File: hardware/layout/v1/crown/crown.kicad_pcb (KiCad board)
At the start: 4 copper layers, 41 x 56 mm, 46 parts, among them J1 Main board, J2 XD_NORTH, J3 XD_EAST, J4 XD_SOUTH, J5 XD_WEST, J6 PIEZO_RAIN, U1 SN74LVC2G04, U2 CD4052BM96, U3 TLV9062IDR, U4 LM393DR2G, U5 TLV9062IDR, U6 LTR-390UV-01, U7 VEML7700-TT, U8 LIS2MDLTR

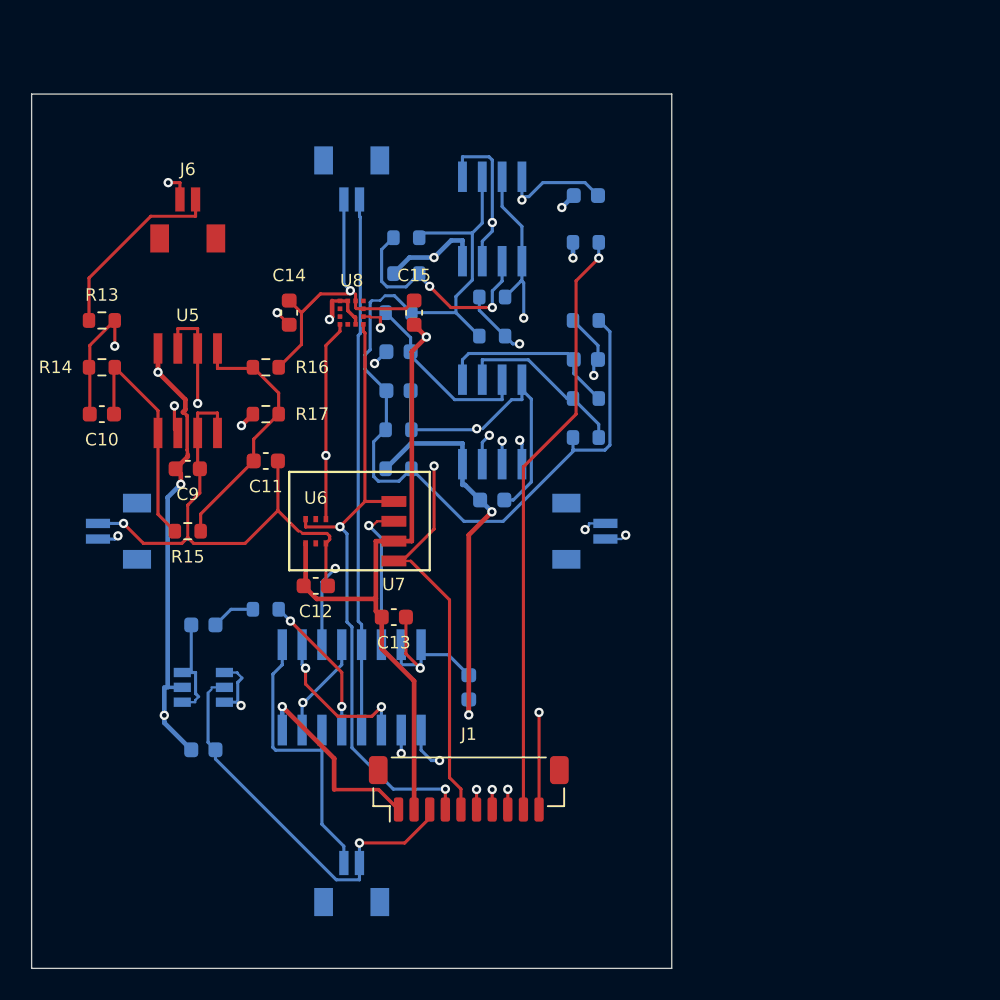
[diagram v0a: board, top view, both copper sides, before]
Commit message: Update project documentation and refactor crown sensor board circuit implementation
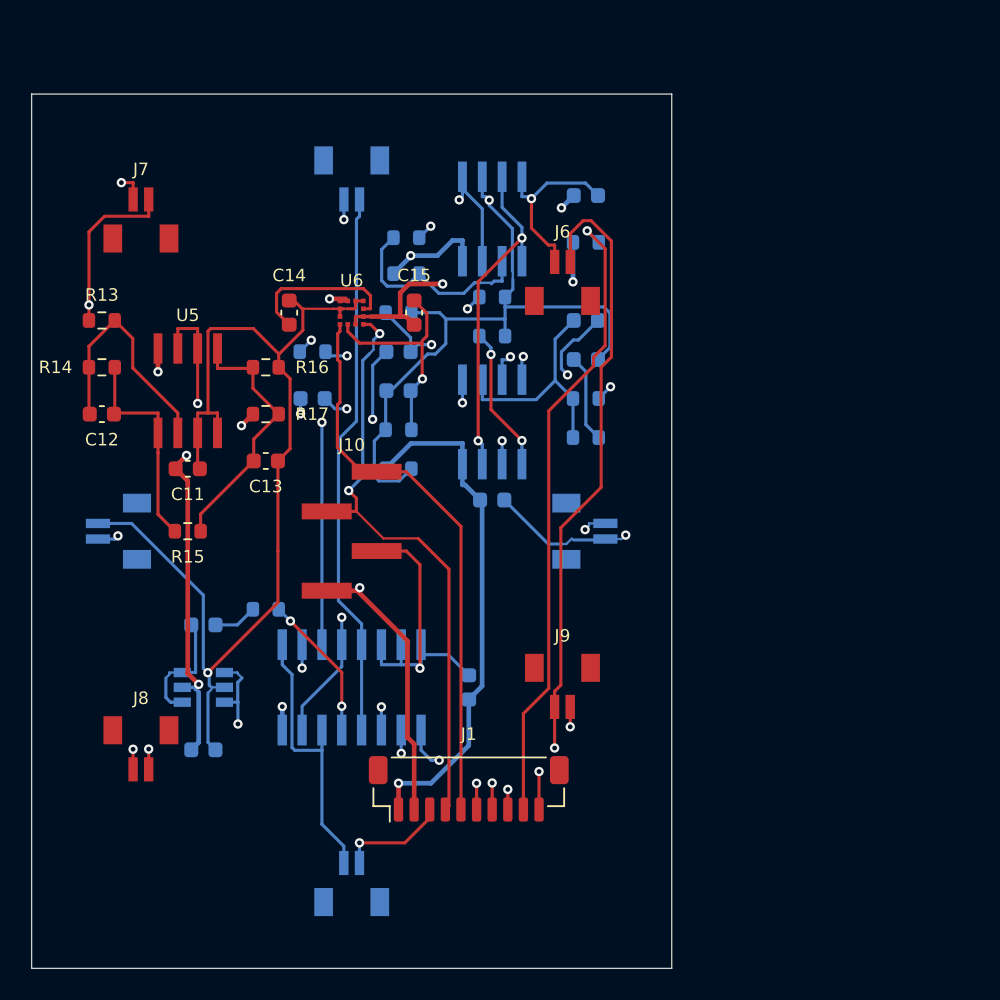
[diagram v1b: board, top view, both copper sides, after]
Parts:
- removed U7: VEML7700-TT, gateway_fp:Vishay_VEML7700-TT
- removed U8: LIS2MDLTR, gateway_fp:ST_LIS2MDLTR_LGA-12
- added J10: DOME_RISER, gateway_fp:HX_PZ2.54-1x4P-SMD, F.Cu at (20.5, -28.0)
- added J7: PIEZO_NW, gateway_fp:JST_BM02B-SRSS-TB, F.Cu at (7.00, -48.0)
- added J8: PIEZO_SW, gateway_fp:JST_BM02B-SRSS-TB, F.Cu at (7.00, -14.0)
- added J9: PIEZO_SE, gateway_fp:JST_BM02B-SRSS-TB, F.Cu at (34.0, -18.0)
- C10: value 47n 50V -> 100n 50V; moved to B.Cu
- C11: value 220n 50V -> 100n 50V
- C12, C8: value 100n 50V -> 18p C0G 50V
- C13: value 100n 50V -> 220n 50V
- C5: value 47n 50V -> 100n 50V
- C6: value 100n 50V -> 47n 50V
- C9: value 100n 50V -> 47n 50V; moved to B.Cu
- J2: value XD_NORTH -> XD_North
- J3: value XD_EAST -> XD_East
- J4: value XD_SOUTH -> XD_South
- J5: value XD_WEST -> XD_West
- J6: value PIEZO_RAIN -> PIEZO_NE
- U1: value SN74LVC2G04 -> SN74LVC2G04DBVR
- U6: value LTR-390UV-01 -> LIS2MDLTR; footprint gateway_fp:LiteOn_LTR-390UV-01 -> gateway_fp:ST_LIS2MDLTR_LGA-12
- moved C10 34.0 mm to (35.5, -49.5)
- moved J6 24.3 mm to (34.0, -44.0)
- moved C12 17.6 mm to (4.50, -35.5)
- moved U6 14.2 mm to (20.5, -42.0)
- moved C13 12.9 mm to (15.0, -32.5)
- moved R9 12.0 mm to (18.0, -39.5)
- moved C5 11.2 mm to (29.5, -30.0)
- moved C6 11.2 mm to (23.5, -39.5)
- moved C9 9.18 mm to (18.0, -36.5)
- moved C8 8.00 mm to (35.5, -41.5)
- moved R7 6.08 mm to (29.5, -40.5)
- moved C11 5.02 mm to (10.0, -32.0)
- moved R8 2.50 mm to (29.5, -43.0)
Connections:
- C10 pad 1: PIEZO_INV -> +5V
- C10 pad 2: PIEZO_STG1 -> GND
- C11 pad 1: PIEZO_ENV -> +5V
- C12 pad 1: +3V3 -> PIEZO_INV
- C12 pad 2: GND -> PIEZO_STG1
- C13 pad 1: +3V3 -> PIEZO_ENV
- C5 pad 1: US_RX_MUX -> +5V
- C5 pad 2: US_AMP1_IN -> GND
- C6 pad 1: +5V -> US_RX_MUX
- C6 pad 2: GND -> US_AMP1_IN
- C7 pad 1: US_AMP1_OUT -> N$2
- C7 pad 2: US_AMP2_IN -> US_VREF
- C8 pad 1: +5V -> US_AMP1_FB
- C8 pad 2: GND -> US_AMP1_OUT
- C9 pad 1: +5V -> US_AMP1_OUT
- C9 pad 2: GND -> US_AMP2_IN
- R5 pad 1: US_VREF -> US_AMP1_FB
- R5 pad 2: US_AMP1_FB -> N$2
- R8 pad 1: US_VREF -> US_AMP2_FB
- R8 pad 2: US_AMP2_FB -> US_VREF
- U6 pad 1: +3V3 -> I2C_SCL
- U6 pad 2: (no net) -> GND
- U6 pad 3: GND -> +3V3
- U6 pad 4: I2C_SCL -> I2C_SDA
- U6 pad 5: (no net) -> +3V3
- U6 pad 6: I2C_SDA -> LIS_C1
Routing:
- net PIEZO_IN: track 12.3 -> 112.1 mm, vias 0 -> 3
- net US_AMP1_OUT: track 11.9 -> 37.0 mm, vias 0 -> 4
- net RAIN_ADC: track 60.3 -> 44.6 mm
- net US_VREF: track 61.5 -> 48.4 mm, vias 0 -> 2
- net US_AMP2_OUT: track 21.6 -> 33.9 mm, vias 2 -> 3
- net US_AMP2_FB: track 12.5 -> 24.3 mm, vias 2 -> 3
- net US_AMP2_IN: track 12.3 -> 24.1 mm, vias 2 -> 3
- net +5V: track 126.3 -> 116.5 mm, vias 8 -> 7
- net I2C_SCL: track 45.3 -> 36.2 mm, vias 2 -> 0
- net GND: track 127.7 -> 134.9 mm, vias 9 -> 11
- net N$2: track 0.00 -> 5.66 mm
- net +3V3: track 75.9 -> 72.0 mm, vias 4 -> 5
- net US_AMP1_FB: track 11.3 -> 14.9 mm
- net XD_E: track 30.8 -> 27.7 mm
- net I2C_SDA: track 41.1 -> 38.6 mm
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
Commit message: Update documentation to reflect hardware specification changes and component substitutions
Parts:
- removed C15: 100n 50V, Capacitor_SMD:C_0603_1608Metric
- C14: value 220n 50V -> 100n 50V
- J10: value DOME_RISER -> DOME_SOCKET
- U6: value LIS2MDLTR -> MMC5603NJ; footprint gateway_fp:ST_LIS2MDLTR_LGA-12 -> gateway_fp:MEMSIC_MMC5603NJ_WLCSP-4
- moved C14 7.50 mm to (24.0, -42.0)
- turned J10 to 0 degrees
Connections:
- C14 pad 1: LIS_C1 -> +3V3
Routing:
- net GND: track 134.9 -> 113.5 mm, vias 11 -> 13
- net +3V3: track 72.0 -> 60.6 mm, vias 5 -> 3
- net LIS_C1: track 9.97 -> 0.00 mm
- net XD_E: track 27.7 -> 36.2 mm
- net RAIN_ADC: track 44.6 -> 51.6 mm
- net US_VREF: track 48.4 -> 55.2 mm, vias 2 -> 3
- net I2C_SDA: track 38.6 -> 34.3 mm, vias 2 -> 0
- net US_AMP2_OUT: track 33.9 -> 38.0 mm
- net US_AMP1_OUT: track 37.0 -> 32.8 mm, vias 4 -> 2
- net +5V: track 116.5 -> 120.4 mm, vias 7 -> 9
- net PIEZO_ENV: track 16.8 -> 19.4 mm
- net US_AMP2_FB: track 24.3 -> 26.8 mm
- net US_AMP1_IN: track 12.0 -> 10.5 mm, vias 2 -> 0
- net US_RX_MUX: track 22.3 -> 21.0 mm
- net I2C_SCL: track 36.2 -> 35.1 mm
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
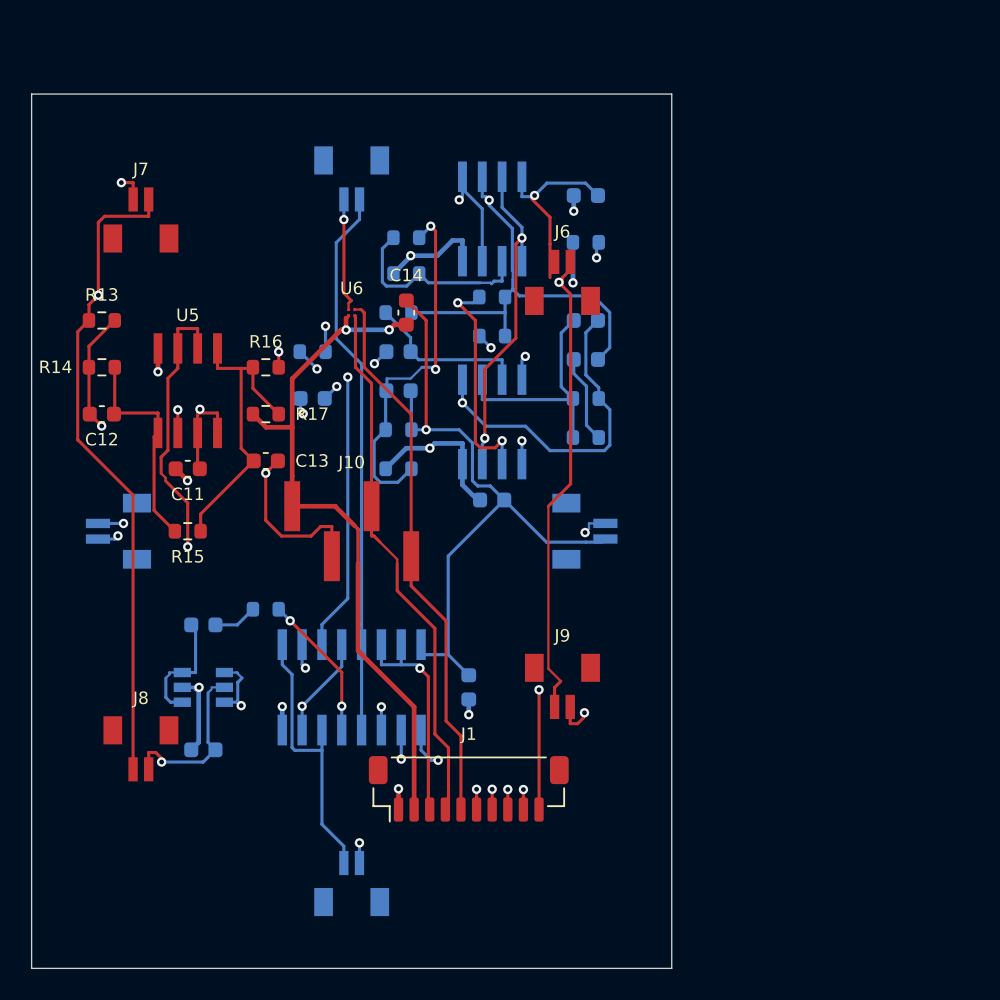
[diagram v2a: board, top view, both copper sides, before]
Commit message: Redesign crown PCB
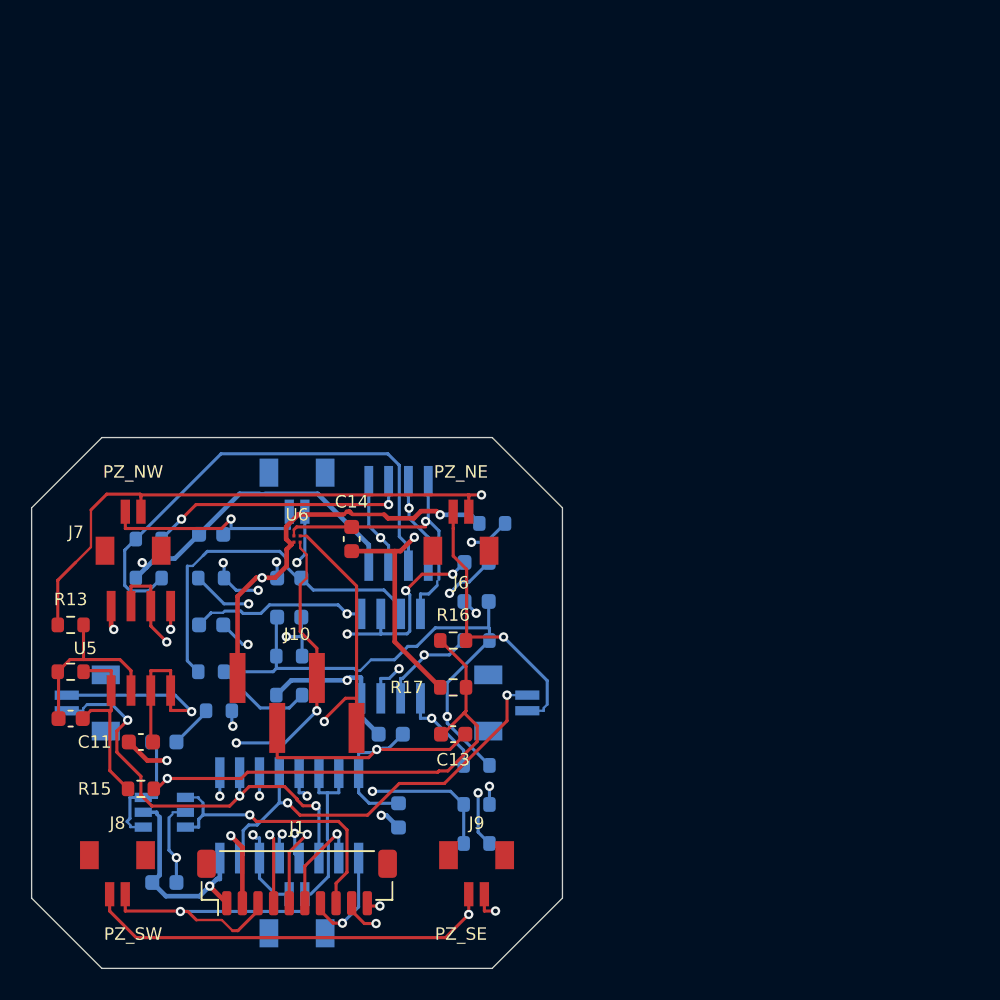
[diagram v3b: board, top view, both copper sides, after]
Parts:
- moved C10 32.4 mm to (11.5, -27.8)
- moved R7 27.5 mm to (28.5, -13.0)
- moved R5 26.9 mm to (28.5, -8.00)
- moved R6 26.9 mm to (28.5, -10.5)
- moved R4 25.9 mm to (11.5, -19.0)
- moved R10 25.5 mm to (7.50, -25.0)
- moved R11 25.4 mm to (7.50, -27.5)
- moved R8 22.0 mm to (28.5, -21.0)
- moved C13 21.2 mm to (27.0, -15.0)
- moved R16 21.2 mm to (27.0, -21.0)
- moved R17 21.2 mm to (27.0, -18.0)
- moved U4 20.4 mm to (23.5, -28.5)
- moved J2 20.3 mm to (17.0, -30.5)
- moved J7 20.0 mm to (6.50, -28.0)
- moved C12 19.6 mm to (2.50, -16.0)
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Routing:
- net PIEZO_ENV: track 19.4 -> 43.5 mm, vias 0 -> 2
- net +5V: track 120.4 -> 100.0 mm, vias 9 -> 6
- net US_VTH: track 12.9 -> 32.2 mm
- net US_VREF: track 55.2 -> 73.6 mm
- net PIEZO_IN: track 111.5 -> 93.7 mm
- net GND: track 113.5 -> 130.9 mm, vias 13 -> 9
- net US_AMP1_FB: track 15.2 -> 32.0 mm, vias 0 -> 4
- net RAIN_ADC: track 51.6 -> 37.0 mm
- net US_AMP1_IN: track 10.5 -> 23.4 mm
- net N$2: track 5.66 -> 18.1 mm, vias 0 -> 2
- net XD_N: track 35.3 -> 25.1 mm, vias 0 -> 3
- net US_AMP2_IN: track 23.6 -> 33.7 mm, vias 3 -> 2
- net XD_E: track 36.2 -> 27.2 mm
- net US_AMP1_OUT: track 32.8 -> 40.5 mm, vias 2 -> 3
- net XD_S: track 17.9 -> 10.3 mm, vias 0 -> 2
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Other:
- board size 41 x 56 mm -> 34 x 34 mm
- board text added: "PZ_NE"
- board text added: "PZ_NW"
- board text added: "PZ_SE"
- board text added: "PZ_SW"
- board text added: "US_E"
- board text added: "US_N"
- board text added: "US_S"
- board text added: "US_W"

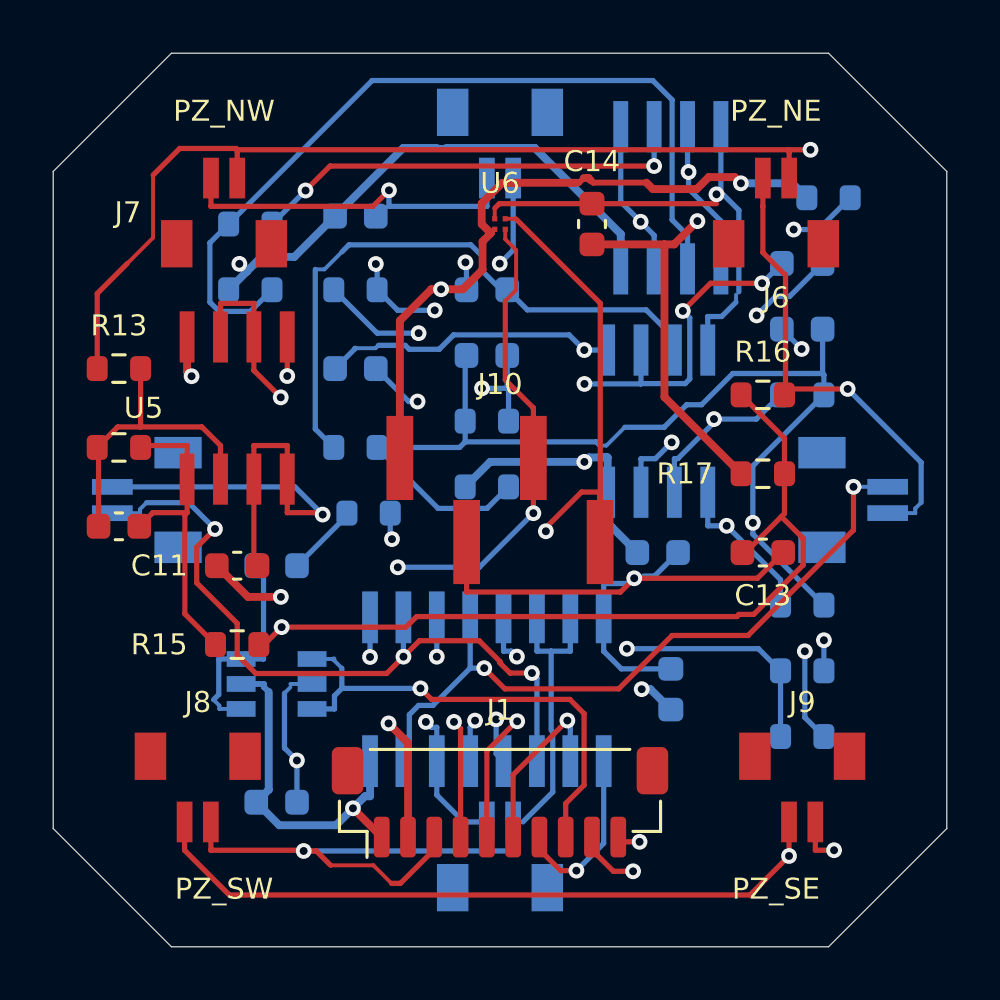
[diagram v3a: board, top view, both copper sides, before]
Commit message: Move all 10 connectors to top layer and reorganize component placement for improved assembly
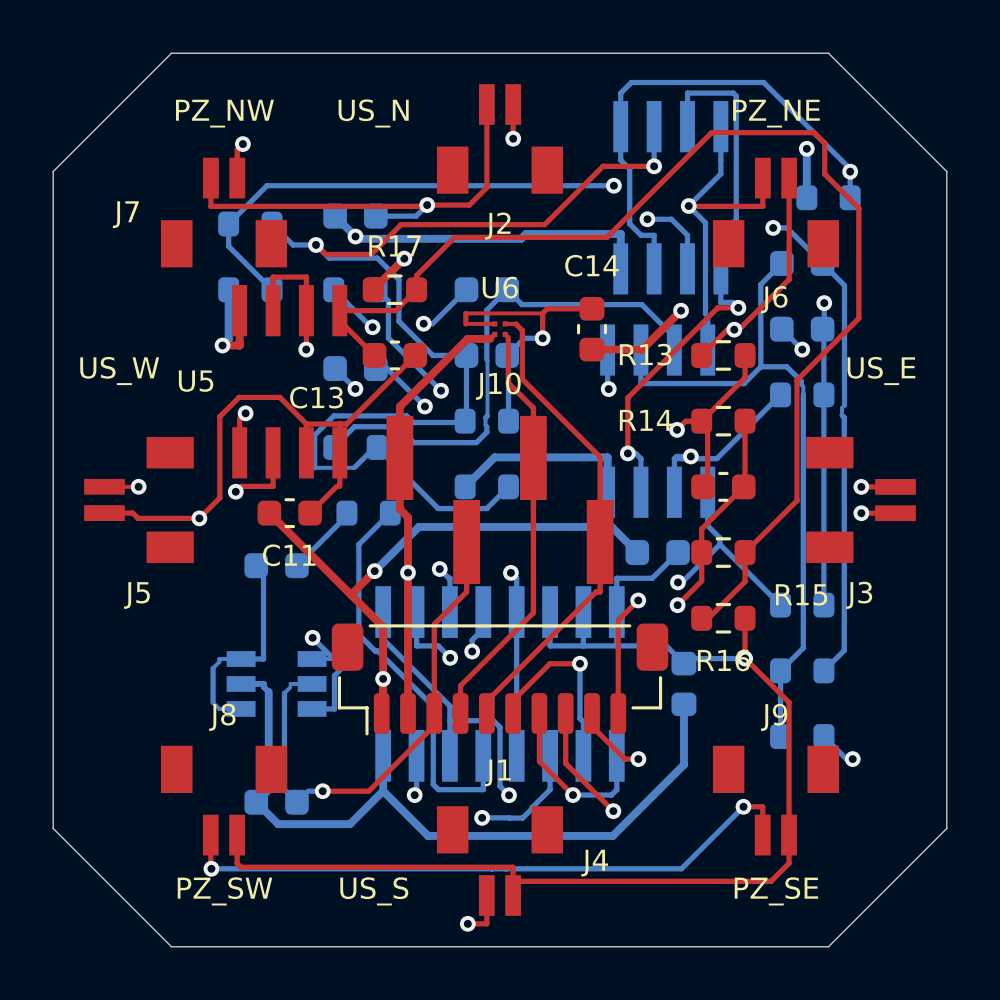
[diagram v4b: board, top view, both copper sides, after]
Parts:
- J2, J3, J4, J5: moved to F.Cu
- moved C12 23.0 mm to (25.5, -17.5)
- moved R14 23.0 mm to (25.5, -20.0)
- moved R13 23.0 mm to (25.5, -22.5)
- moved R15 18.8 mm to (25.5, -15.0)
- moved C13 15.9 mm to (13.0, -22.5)
- moved R17 15.7 mm to (13.0, -25.0)
- moved R16 8.63 mm to (25.5, -12.5)
- moved J1 4.70 mm to (17.0, -10.2)
- moved C14 4.00 mm to (20.5, -23.5)
- moved U6 4.00 mm to (17.0, -23.5)
- moved C11 2.83 mm to (9.00, -16.5)
- moved U5 2.24 mm to (9.00, -21.5)
- moved J8 1.12 mm to (6.50, -5.50)
- moved J9 1.12 mm to (27.5, -5.50)
- moved C3 0.54 mm to (24.0, -10.0)
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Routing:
- net PIEZO_INV: track 11.8 -> 37.4 mm, vias 0 -> 2
- net PIEZO_STG1: track 11.9 -> 30.9 mm, vias 0 -> 2
- net XD_E: track 27.2 -> 41.5 mm, vias 2 -> 3
- net I2C_SCL: track 31.3 -> 18.4 mm, vias 2 -> 0
- net I2C_SDA: track 28.9 -> 16.0 mm, vias 3 -> 0
- net US_AMP2_IN: track 33.7 -> 22.5 mm
- net XD_N: track 25.1 -> 34.9 mm, vias 3 -> 2
- net US_VTH: track 32.2 -> 23.3 mm, vias 0 -> 2
- net US_TX: track 18.4 -> 26.9 mm, vias 1 -> 2
- net XD_S: track 10.3 -> 18.6 mm
- net PIEZO_IN: track 93.7 -> 85.6 mm, vias 2 -> 4
- net +3V3: track 65.9 -> 57.9 mm
- net XD_W: track 27.8 -> 35.7 mm
- net US_AMP2_OUT: track 41.2 -> 34.6 mm, vias 4 -> 3
- net RAIN_ADC: track 37.0 -> 30.4 mm
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
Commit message: Add silkscreen connector labels to all PCB variants for improved assembly identification
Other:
- board text added: "DOME"
- board text added: "MAIN"
